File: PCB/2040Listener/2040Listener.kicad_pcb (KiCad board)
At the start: 2 copper layers, 73 x 34.5 mm, 33 parts, among them J1 CONN4_292303_SOCKET, J2 USB-AP-S-RA-PLUG, SW1 PTS815 SJM 250 SMTR LFS, SW2 PTS815 SJM 250 SMTR LFS, U1 RP2040, U2 NCP1117-3.3_SOT223, U4 BY25Q16AWTIG(R), Y1 ABM8-272-T3

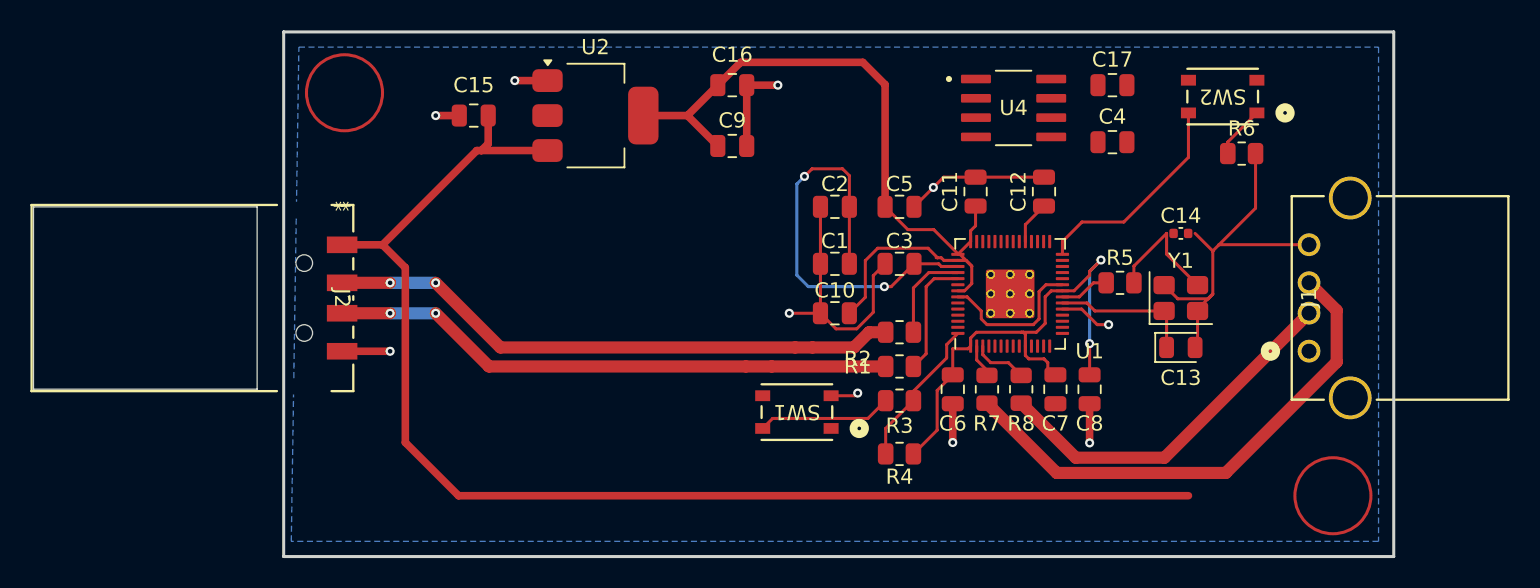
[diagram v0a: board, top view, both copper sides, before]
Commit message: reposition elements for better routing
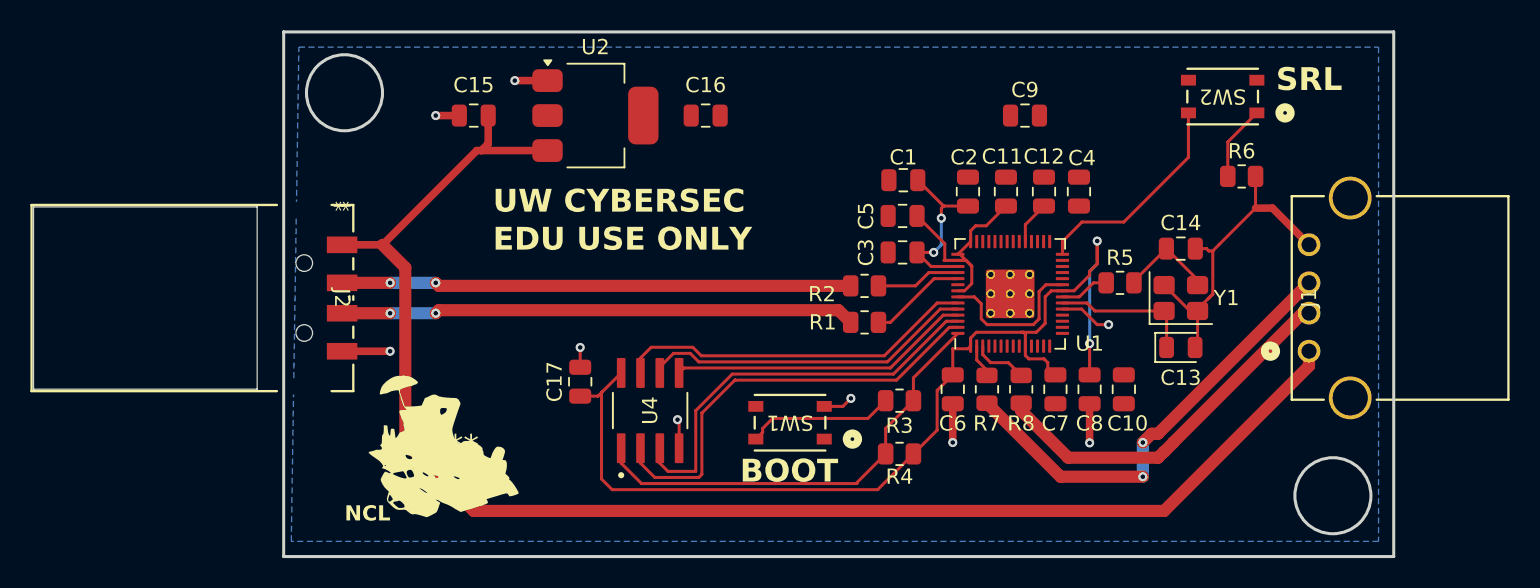
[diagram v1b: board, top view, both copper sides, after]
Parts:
- added G***: LOGO, LOGO, F.Cu at (109.0, 76.8)
- C14: footprint Capacitor_SMD:C_0402_1005Metric -> Capacitor_SMD:C_0805_2012Metric
- moved C17 40.1 mm to (118.0, 72.5), turned to 90 degrees
- moved U4 31.1 mm to (122.6, 74.4), turned to 90 degrees
- moved C10 19.6 mm to (153.8, 73.0), turned to -90 degrees
- moved C9 19.4 mm to (147.2, 55.0)
- moved C2 8.81 mm to (143.5, 60.0), turned to 90 degrees
- moved C1 7.11 mm to (139.2, 59.2)
- moved C4 3.92 mm to (150.8, 60.0), turned to 90 degrees
- moved R2 3.82 mm to (136.7, 66.2)
- moved R1 3.70 mm to (136.7, 68.6)
- moved C16 2.66 mm to (126.2, 55.0)
- moved C11 2.00 mm to (146.0, 60.0)
- moved R6 1.50 mm to (161.5, 59.0)
- moved C14 1.00 mm to (157.5, 63.8)
- moved SW1 0.83 mm to (131.8, 75.2)
- moved C3 0.78 mm to (139.2, 64.0)
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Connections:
- U4 pad 1: unconnected-(U4-/CS-Pad1) -> /QSPI_SS
- U4 pad 2: unconnected-(U4-IO1-Pad2) -> /QSPI_SD1
- U4 pad 3: unconnected-(U4-IO2-Pad3) -> /QSPI_SD2
- U4 pad 4: unconnected-(U4-VSS-Pad4) -> GND
- U4 pad 5: unconnected-(U4-SI-Pad5) -> /QSPI_SD0
- U4 pad 6: unconnected-(U4-SCL-Pad6) -> /QSPI_SCLK
- U4 pad 7: unconnected-(U4-IO3-Pad7) -> /QSPI_SD3
- U4 pad 8: unconnected-(U4-VCC-Pad8) -> +3V3
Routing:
- net GND: track 76.6 -> 44.0 mm, vias 10 -> 9
- net /QSPI_SD1: track 0.00 -> 28.7 mm
- net /QSPI_SD2: track 0.00 -> 27.2 mm
- net /QSPI_SD3: track 0.00 -> 23.8 mm
- net /QSPI_SCLK: track 0.00 -> 22.0 mm
- net /QSPI_SD0: track 0.00 -> 19.9 mm
- net /QSPI_SS: track 9.89 -> 29.7 mm
- net +1V1: track 37.5 -> 21.8 mm
- net VBUS: track 85.1 -> 98.4 mm
- net +3V3: track 90.7 -> 85.0 mm
- net /USB_D-: track 37.9 -> 33.5 mm
- net /GPIO0: track 33.9 -> 29.8 mm, vias 0 -> 2
- net /USB_D+: track 37.2 -> 33.9 mm
- net Net-(C14-Pad1): track 8.38 -> 6.38 mm
- net Net-(R6-Pad1): track 3.47 -> 4.97 mm
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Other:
- outline, holes or cut-outs redrawn
- board text added: "BOOT"
- board text added: "EDU USE ONLY"
- board text added: "NCL"
- board text added: "SRL"
- board text added: "UW CYBERSEC"

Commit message: first gerber
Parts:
- C14: footprint Capacitor_SMD:C_0805_2012Metric -> Capacitor_SMD:C_0402_1005Metric
- J2: footprint Library:CONN_USB-AP-S-RA-SMT_ADM -> Library:USBAPSRA
- moved J2 12.3 mm to (104.4, 63.9)
- moved C9 6.90 mm to (151.9, 60.1)
- moved C4 4.66 mm to (153.5, 63.8), turned to 0 degrees
- moved G*** 2.33 mm to (111.3, 76.4)
- moved C11 0.30 mm to (146.0, 60.3)
- moved C12 0.30 mm to (148.5, 60.3)
- moved C2 0.30 mm to (143.5, 60.3)
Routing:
- net GND: track 44.0 -> 65.3 mm, vias 9 -> 13
- net +3V3: track 85.0 -> 75.2 mm, vias 2 -> 1
- net +1V1: track 21.8 -> 31.6 mm, vias 2 -> 5
- net /USB_D-: track 33.5 -> 31.7 mm, vias 2 -> 1
- net /USB_D+: track 33.9 -> 32.2 mm, vias 2 -> 1
- added copper zone on F.Cu, net +3V3

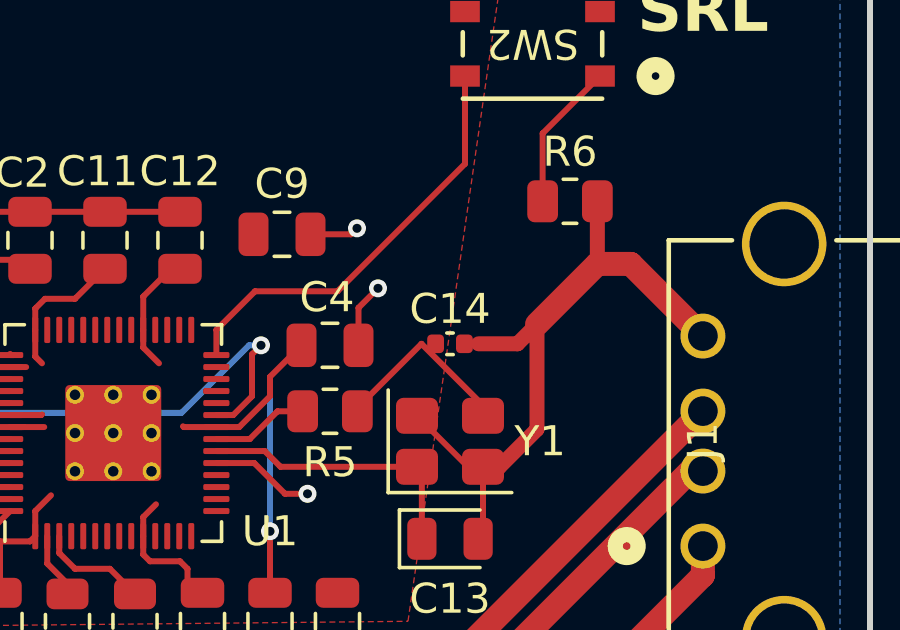
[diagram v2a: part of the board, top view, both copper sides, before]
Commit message: fix small footprint
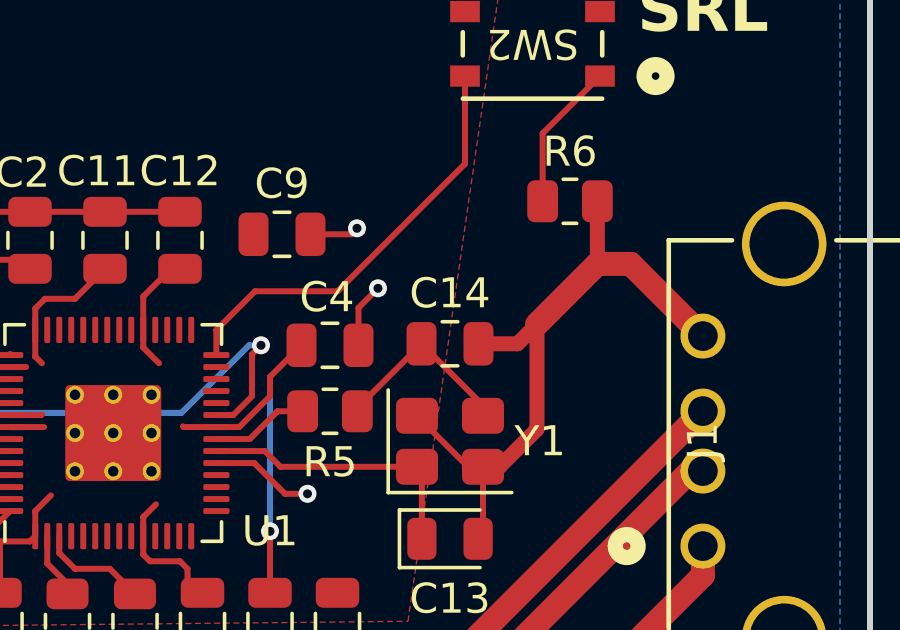
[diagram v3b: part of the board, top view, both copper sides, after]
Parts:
- C14: footprint Capacitor_SMD:C_0402_1005Metric -> Capacitor_SMD:C_0805_2012Metric
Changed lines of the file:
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@@
 			(drillshape 0)
 			(scaleselection 1)
-			(outputdirectory "")
+			(outputdirectory "fab/")
 		)
 	)
@@
 		)
 	)
-	(footprint "Capacitor_SMD:C_0402_1005Metric"
+	(footprint "Capacitor_SMD:C_0805_2012Metric"
 		(layer "F.Cu")
 		(at 157.5 63.75)
-		(descr "Capacitor SMD 0402 (1005 Metric), square (rectangular) end terminal, IPC-7351 nominal, (Body size source: IPC-SM-782 page 76, https://www.pcb-3d.com/wordpress/wp-content/uploads/ipc-sm-782a_amendment_1_and_2.pdf), generated with kicad-footprint-generator")
+		(descr "Capacitor SMD 0805 (2012 Metric), square (rectangular) end terminal, IPC-7351 nominal, (Body size source: IPC-SM-782 page 76, https://www.pcb-3d.com/wordpress/wp-content/uploads/ipc-sm-782a_amendment_1_and_2.pdf, https://docs.google.com/spreadsheets/d/1BsfQQcO9C6DZCsRaXUlFlo91Tg2WpOkGARC1WS5S8t0/edit?usp=sharing), generated with kicad-footprint-generator")
 		(tags "capacitor")
 		(property "Reference" "C14"
-			(at 0 -1.16 0)
+			(at 0 -1.68 0)
 			(layer "F.SilkS")
 			(effects
@@
 		)
 		(property "Value" "15p"
-			(at 0 1.16 0)
-			(layer "F.Fab")
-			(effects
-				(font
-					(size 1 1)
-					(thickness 0.15)
-				)
-			)
-		)
-		(property "Datasheet" "~"
+			(at 0 1.68 0)
+			(layer "F.Fab")
+			(effects
+				(font
+					(size 1 1)
+					(thickness 0.15)
+				)
+			)
+		)
+		(property "Datasheet" ""
 			(at 0 0 0)
 			(layer "F.Fab")
@@
 		(attr smd)
 		(fp_line
-			(start -0.107836 -0.36)
-			(end 0.107836 -0.36)
+			(start -0.261252 -0.735)
+			(end 0.261252 -0.735)
 			(stroke
 				(width 0.12)
@@
 		)
 		(fp_line
-			(start -0.107836 0.36)
-			(end 0.107836 0.36)
+			(start -0.261252 0.735)
+			(end 0.261252 0.735)
 			(stroke
 				(width 0.12)
@@
 		)
 		(fp_line
-			(start -0.91 -0.46)
-			(end 0.91 -0.46)
-			(stroke
-				(width 0.05)
-				(type solid)
-			)
-			(layer "F.CrtYd")
-		)
-		(fp_line
-			(start -0.91 0.46)
-			(end -0.91 -0.46)
-			(stroke
-				(width 0.05)
-				(type solid)
-			)
-			(layer "F.CrtYd")
-		)
-		(fp_line
-			(start 0.91 -0.46)
-			(end 0.91 0.46)
-			(stroke
-				(width 0.05)
-				(type solid)
-			)
-			(layer "F.CrtYd")
-		)
-		(fp_line
-			(start 0.91 0.46)
-			(end -0.91 0.46)
-			(stroke
-				(width 0.05)
-				(type solid)
-			)
-			(layer "F.CrtYd")
-		)
-		(fp_line
-			(start -0.5 -0.25)
-			(end 0.5 -0.25)
-			(stroke
-				(width 0.1)
-				(type solid)
-			)
-			(layer "F.Fab")
-		)
-		(fp_line
-			(start -0.5 0.25)
-			(end -0.5 -0.25)
-			(stroke
-				(width 0.1)
-				(type solid)
-			)
-			(layer "F.Fab")
-		)
-		(fp_line
-			(start 0.5 -0.25)
-			(end 0.5 0.25)
-			(stroke
-				(width 0.1)
-				(type solid)
-			)
-			(layer "F.Fab")
-		)
-		(fp_line
-			(start 0.5 0.25)
-			(end -0.5 0.25)
+			(start -1.7 -0.98)
+			(end 1.7 -0.98)
+			(stroke
+				(width 0.05)
+				(type solid)
+			)
+			(layer "F.CrtYd")
+		)
+		(fp_line
+			(start -1.7 0.98)
+			(end -1.7 -0.98)
+			(stroke
+				(width 0.05)
+				(type solid)
+			)
+			(layer "F.CrtYd")
+		)
+		(fp_line
+			(start 1.7 -0.98)
+			(end 1.7 0.98)
+			(stroke
+				(width 0.05)
+				(type solid)
+			)
+			(layer "F.CrtYd")
+		)
+		(fp_line
+			(start 1.7 0.98)
+			(end -1.7 0.98)
+			(stroke
+				(width 0.05)
+				(type solid)
+			)
+			(layer "F.CrtYd")
+		)
+		(fp_line
+			(start -1 -0.625)
+			(end 1 -0.625)
+			(stroke
+				(width 0.1)
+				(type solid)
+			)
+			(layer "F.Fab")
+		)
+		(fp_line
+			(start -1 0.625)
+			(end -1 -0.625)
+			(stroke
+				(width 0.1)
+				(type solid)
+			)
+			(layer "F.Fab")
+		)
+		(fp_line
+			(start 1 -0.625)
+			(end 1 0.625)
+			(stroke
+				(width 0.1)
+				(type solid)
+			)
+			(layer "F.Fab")
+		)
+		(fp_line
+			(start 1 0.625)
+			(end -1 0.625)
 			(stroke
 				(width 0.1)
@@
 			(effects
 				(font
-					(size 0.25 0.25)
-					(thickness 0.04)
+					(size 0.5 0.5)
+					(thickness 0.08)
 				)
 			)
 		)
 		(pad "1" smd roundrect
-			(at -0.48 0)
-			(size 0.56 0.62)
+			(at -0.95 0)
+			(size 1 1.45)
 			(layers "F.Cu" "F.Mask" "F.Paste")
 			(roundrect_rratio 0.25)
@@
 		)
 		(pad "2" smd roundrect
-			(at 0.48 0)
-			(size 0.56 0.62)
+			(at 0.95 0)
+			(size 1 1.45)
 			(layers "F.Cu" "F.Mask" "F.Paste")
 			(roundrect_rratio 0.25)
@@
 		)
 		(embedded_fonts no)
-		(model "${KICAD9_3DMODEL_DIR}/Capacitor_SMD.3dshapes/C_0402_1005Metric.step"
+		(model "${KICAD9_3DMODEL_DIR}/Capacitor_SMD.3dshapes/C_0805_2012Metric.step"
 			(offset
 				(xyz 0 0 0)
